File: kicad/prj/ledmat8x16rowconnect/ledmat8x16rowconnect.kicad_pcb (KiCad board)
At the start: 2 copper layers, 15.9 x 63.8 mm, 2 parts, among them J1 Conn_02x08_Odd_Even, J2 Conn_02x08_Odd_Even

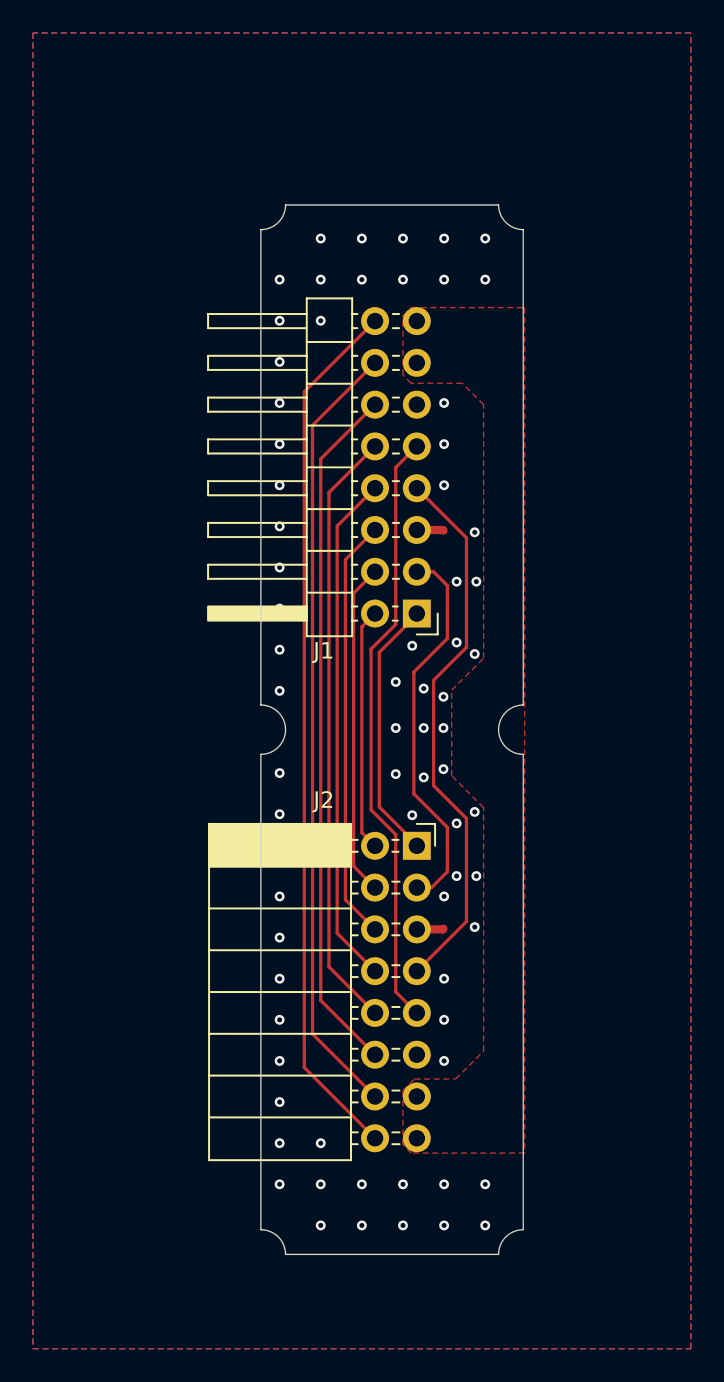
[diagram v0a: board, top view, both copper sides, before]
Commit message: Add dimensions to interconnect board, fix silkscreen
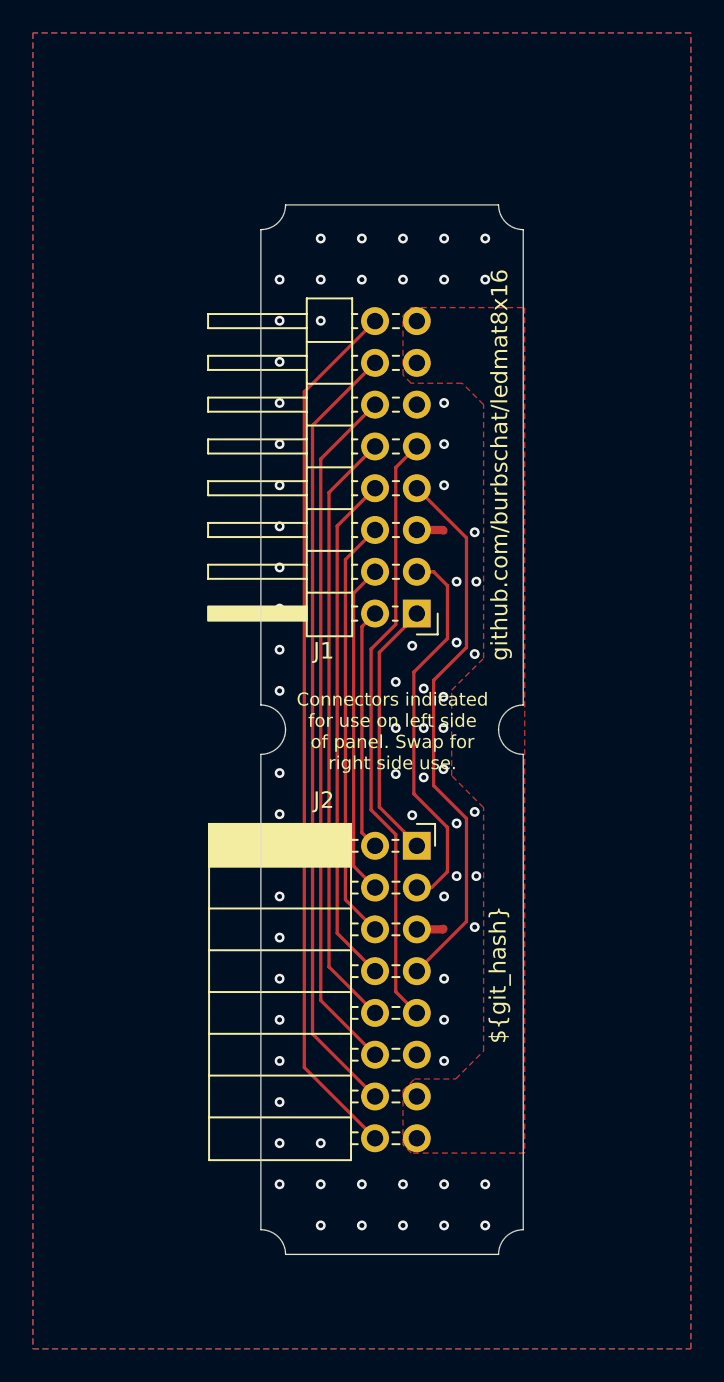
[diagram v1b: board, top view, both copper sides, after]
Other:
- board text added: "Connectors indicated for use on left side of panel. Swap for right side use."
